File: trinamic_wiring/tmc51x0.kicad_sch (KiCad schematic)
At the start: 0 parts

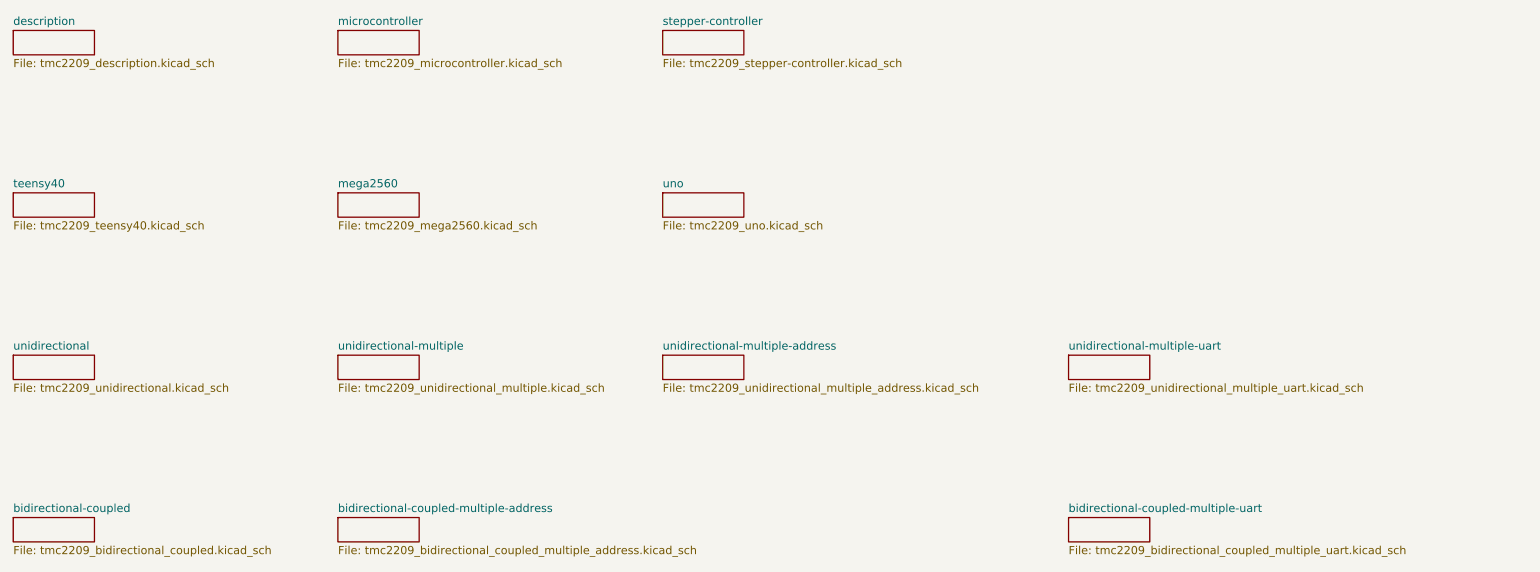
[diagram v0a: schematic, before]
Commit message: Add TMC51X0 files
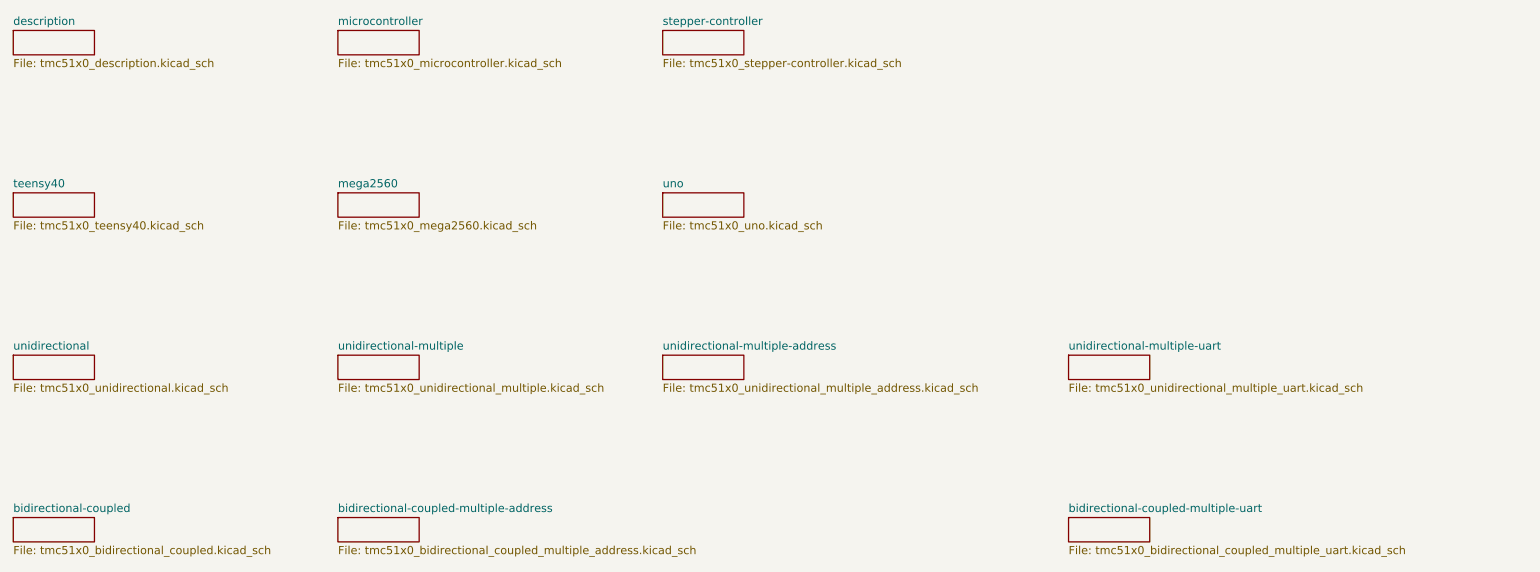
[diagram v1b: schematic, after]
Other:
- sheet bidirectional-coupled: file tmc2209_bidirectional_coupled.kicad_sch -> tmc51x0_bidirectional_coupled.kicad_sch
- sheet bidirectional-coupled-multiple-address: file tmc2209_bidirectional_coupled_multiple_address.kicad_sch -> tmc51x0_bidirectional_coupled_multiple_address.kicad_sch
- sheet bidirectional-coupled-multiple-uart: file tmc2209_bidirectional_coupled_multiple_uart.kicad_sch -> tmc51x0_bidirectional_coupled_multiple_uart.kicad_sch
- sheet description: file tmc2209_description.kicad_sch -> tmc51x0_description.kicad_sch
- sheet mega2560: file tmc2209_mega2560.kicad_sch -> tmc51x0_mega2560.kicad_sch
- sheet microcontroller: file tmc2209_microcontroller.kicad_sch -> tmc51x0_microcontroller.kicad_sch
- sheet stepper-controller: file tmc2209_stepper-controller.kicad_sch -> tmc51x0_stepper-controller.kicad_sch
- sheet teensy40: file tmc2209_teensy40.kicad_sch -> tmc51x0_teensy40.kicad_sch
- sheet unidirectional: file tmc2209_unidirectional.kicad_sch -> tmc51x0_unidirectional.kicad_sch
- sheet unidirectional-multiple: file tmc2209_unidirectional_multiple.kicad_sch -> tmc51x0_unidirectional_multiple.kicad_sch
- sheet unidirectional-multiple-address: file tmc2209_unidirectional_multiple_address.kicad_sch -> tmc51x0_unidirectional_multiple_address.kicad_sch
- sheet unidirectional-multiple-uart: file tmc2209_unidirectional_multiple_uart.kicad_sch -> tmc51x0_unidirectional_multiple_uart.kicad_sch
- sheet uno: file tmc2209_uno.kicad_sch -> tmc51x0_uno.kicad_sch
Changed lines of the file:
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@@
       (effects (font (size 1.27 1.27)) (justify left bottom))
     )
-    (property "Sheetfile" "tmc2209_bidirectional_coupled_multiple_uart.kicad_sch" (at 208.28 133.9346 0)
+    (property "Sheetfile" "tmc51x0_bidirectional_coupled_multiple_uart.kicad_sch" (at 208.28 133.9346 0)
       (effects (font (size 1.27 1.27)) (justify left top))
     )
@@
       (effects (font (size 1.27 1.27)) (justify left bottom))
     )
-    (property "Sheetfile" "tmc2209_unidirectional.kicad_sch" (at 43.18 108.5346 0)
+    (property "Sheetfile" "tmc51x0_unidirectional.kicad_sch" (at 43.18 108.5346 0)
       (effects (font (size 1.27 1.27)) (justify left top))
     )
@@
       (effects (font (size 1.27 1.27)) (justify left bottom))
     )
-    (property "Sheetfile" "tmc2209_stepper-controller.kicad_sch" (at 144.78 57.7346 0)
+    (property "Sheetfile" "tmc51x0_stepper-controller.kicad_sch" (at 144.78 57.7346 0)
       (effects (font (size 1.27 1.27)) (justify left top))
     )
@@
       (effects (font (size 1.27 1.27)) (justify left bottom))
     )
-    (property "Sheetfile" "tmc2209_teensy40.kicad_sch" (at 43.18 83.1346 0)
+    (property "Sheetfile" "tmc51x0_teensy40.kicad_sch" (at 43.18 83.1346 0)
       (effects (font (size 1.27 1.27)) (justify left top))
     )
@@
       (effects (font (size 1.27 1.27)) (justify left bottom))
     )
-    (property "Sheetfile" "tmc2209_unidirectional_multiple.kicad_sch" (at 93.98 108.5346 0)
+    (property "Sheetfile" "tmc51x0_unidirectional_multiple.kicad_sch" (at 93.98 108.5346 0)
       (effects (font (size 1.27 1.27)) (justify left top))
     )
@@
       (effects (font (size 1.27 1.27)) (justify left bottom))
     )
-    (property "Sheetfile" "tmc2209_bidirectional_coupled_multiple_address.kicad_sch" (at 93.98 133.9346 0)
+    (property "Sheetfile" "tmc51x0_bidirectional_coupled_multiple_address.kicad_sch" (at 93.98 133.9346 0)
       (effects (font (size 1.27 1.27)) (justify left top))
     )
@@
       (effects (font (size 1.27 1.27)) (justify left bottom))
     )
-    (property "Sheetfile" "tmc2209_uno.kicad_sch" (at 144.78 83.1346 0)
+    (property "Sheetfile" "tmc51x0_uno.kicad_sch" (at 144.78 83.1346 0)
       (effects (font (size 1.27 1.27)) (justify left top))
     )
@@
       (effects (font (size 1.27 1.27)) (justify left bottom))
     )
-    (property "Sheetfile" "tmc2209_description.kicad_sch" (at 43.18 57.7346 0)
+    (property "Sheetfile" "tmc51x0_description.kicad_sch" (at 43.18 57.7346 0)
       (effects (font (size 1.27 1.27)) (justify left top))
     )
@@
       (effects (font (size 1.27 1.27)) (justify left bottom))
     )
-    (property "Sheetfile" "tmc2209_microcontroller.kicad_sch" (at 93.98 57.7346 0)
+    (property "Sheetfile" "tmc51x0_microcontroller.kicad_sch" (at 93.98 57.7346 0)
       (effects (font (size 1.27 1.27)) (justify left top))
     )
@@
       (effects (font (size 1.27 1.27)) (justify left bottom))
     )
-    (property "Sheetfile" "tmc2209_unidirectional_multiple_address.kicad_sch" (at 144.78 108.5346 0)
+    (property "Sheetfile" "tmc51x0_unidirectional_multiple_address.kicad_sch" (at 144.78 108.5346 0)
       (effects (font (size 1.27 1.27)) (justify left top))
     )
@@
       (effects (font (size 1.27 1.27)) (justify left bottom))
     )
-    (property "Sheetfile" "tmc2209_unidirectional_multiple_uart.kicad_sch" (at 208.28 108.5346 0)
+    (property "Sheetfile" "tmc51x0_unidirectional_multiple_uart.kicad_sch" (at 208.28 108.5346 0)
       (effects (font (size 1.27 1.27)) (justify left top))
     )
@@
       (effects (font (size 1.27 1.27)) (justify left bottom))
     )
-    (property "Sheetfile" "tmc2209_bidirectional_coupled.kicad_sch" (at 43.18 133.9346 0)
+    (property "Sheetfile" "tmc51x0_bidirectional_coupled.kicad_sch" (at 43.18 133.9346 0)
       (effects (font (size 1.27 1.27)) (justify left top))
     )
@@
       (effects (font (size 1.27 1.27)) (justify left bottom))
     )
-    (property "Sheetfile" "tmc2209_mega2560.kicad_sch" (at 93.98 83.1346 0)
+    (property "Sheetfile" "tmc51x0_mega2560.kicad_sch" (at 93.98 83.1346 0)
       (effects (font (size 1.27 1.27)) (justify left top))
     )

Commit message: Remove unused sheets
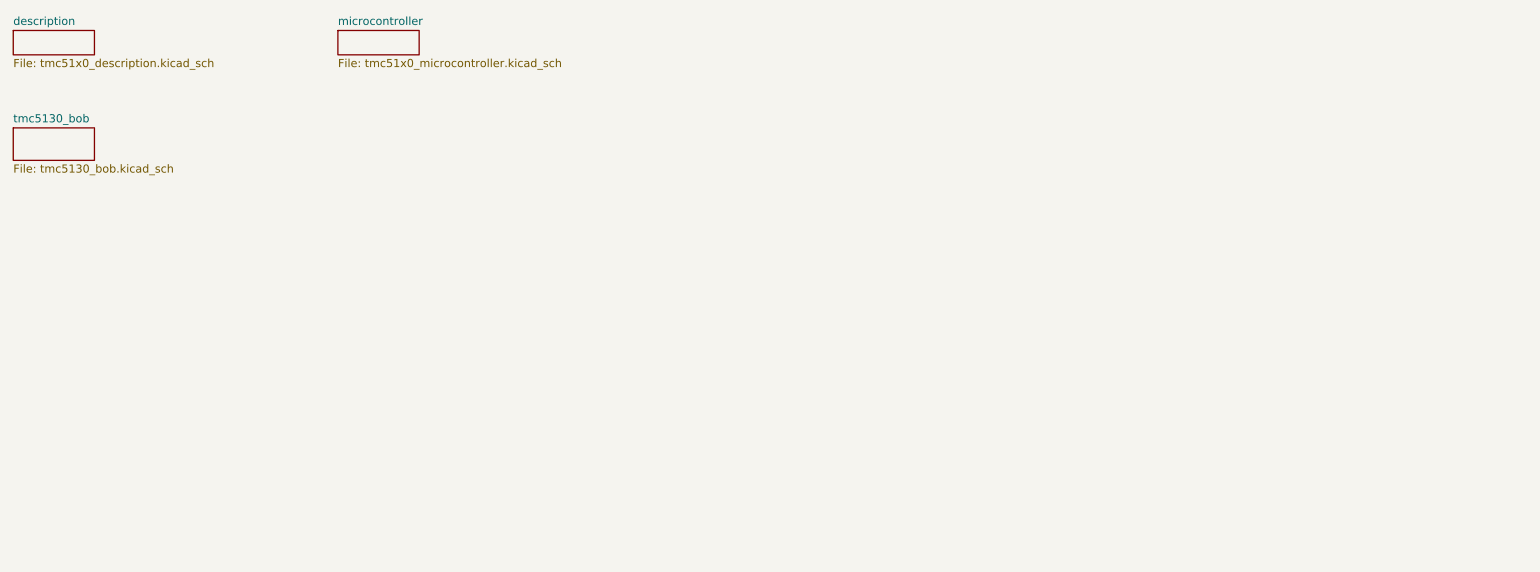
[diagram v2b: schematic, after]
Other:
- removed sheet bidirectional-coupled
- removed sheet bidirectional-coupled-multiple-address
- removed sheet bidirectional-coupled-multiple-uart
- removed sheet mega2560
- removed sheet stepper-controller
- removed sheet teensy40
- removed sheet unidirectional
- removed sheet unidirectional-multiple
- removed sheet unidirectional-multiple-address
- removed sheet unidirectional-multiple-uart
- removed sheet uno
- added sheet tmc5130_bob (tmc5130_bob.kicad_sch)
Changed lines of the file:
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@@
   (title_block
     (title "Trinamic Wiring")
-    (date "2023-08-02")
+    (date "2024-01-31")
     (rev "0.4")
     (company "Janelia Research Campus")
   )
-  (sheet (at 208.28 129.54) (size 12.7 3.81) (fields_autoplaced)
+  (sheet (at 43.18 68.58) (size 12.7 5.08) (fields_autoplaced)
     (stroke (width 0.1524) (type solid))
     (fill (color 0 0 0 0.0000))
-    (property "Sheetname" "bidirectional-coupled-multiple-uart" (at 208.28 128.8284 0)
+    (property "Sheetname" "tmc5130_bob" (at 43.18 67.8684 0)
       (effects (font (size 1.27 1.27)) (justify left bottom))
     )
-    (property "Sheetfile" "tmc51x0_bidirectional_coupled_multiple_uart.kicad_sch" (at 208.28 133.9346 0)
+    (property "Sheetfile" "tmc5130_bob.kicad_sch" (at 43.18 74.2446 0)
       (effects (font (size 1.27 1.27)) (justify left top))
     )
     (instances
       (project "trinamic_wiring"
-        (path "/e4144788-6304-493f-818e-5d881d3b7418/c8eda2b5-ab13-4033-82d9-875c9fcaf884" (page "12"))
-        (path "/e4144788-6304-493f-818e-5d881d3b7418/a161638e-a96f-4455-865a-1d7502675f43" (page "21"))
-      )
-    )
-  )
-  (sheet (at 43.18 104.14) (size 12.7 3.81) (fields_autoplaced)
-    (stroke (width 0.1524) (type solid))
-    (fill (color 0 0 0 0.0000))
-    (property "Sheetname" "unidirectional" (at 43.18 103.4284 0)
-      (effects (font (size 1.27 1.27)) (justify left bottom))
-    )
-    (property "Sheetfile" "tmc51x0_unidirectional.kicad_sch" (at 43.18 108.5346 0)
-      (effects (font (size 1.27 1.27)) (justify left top))
-    )
-    (instances
-      (project "trinamic_wiring"
-        (path "/e4144788-6304-493f-818e-5d881d3b7418/c8eda2b5-ab13-4033-82d9-875c9fcaf884" (page "6"))
-        (path "/e4144788-6304-493f-818e-5d881d3b7418/a161638e-a96f-4455-865a-1d7502675f43" (page "18"))
-      )
-    )
-  )
-  (sheet (at 144.78 53.34) (size 12.7 3.81) (fields_autoplaced)
-    (stroke (width 0.1524) (type solid))
-    (fill (color 0 0 0 0.0000))
-    (property "Sheetname" "stepper-controller" (at 144.78 52.6284 0)
-      (effects (font (size 1.27 1.27)) (justify left bottom))
-    )
-    (property "Sheetfile" "tmc51x0_stepper-controller.kicad_sch" (at 144.78 57.7346 0)
-      (effects (font (size 1.27 1.27)) (justify left top))
-    )
-    (instances
-      (project "trinamic_wiring"
-        (path "/e4144788-6304-493f-818e-5d881d3b7418/c8eda2b5-ab13-4033-82d9-875c9fcaf884" (page "15"))
-        (path "/e4144788-6304-493f-818e-5d881d3b7418/a161638e-a96f-4455-865a-1d7502675f43" (page "28"))
-      )
-    )
-  )
-  (sheet (at 43.18 78.74) (size 12.7 3.81) (fields_autoplaced)
-    (stroke (width 0.1524) (type solid))
-    (fill (color 0 0 0 0.0000))
-    (property "Sheetname" "teensy40" (at 43.18 78.0284 0)
-      (effects (font (size 1.27 1.27)) (justify left bottom))
-    )
-    (property "Sheetfile" "tmc51x0_teensy40.kicad_sch" (at 43.18 83.1346 0)
-      (effects (font (size 1.27 1.27)) (justify left top))
-    )
-    (instances
-      (project "trinamic_wiring"
-        (path "/e4144788-6304-493f-818e-5d881d3b7418/c8eda2b5-ab13-4033-82d9-875c9fcaf884" (page "3"))
-        (path "/e4144788-6304-493f-818e-5d881d3b7418/a161638e-a96f-4455-865a-1d7502675f43" (page "27"))
-      )
-    )
-  )
-  (sheet (at 93.98 104.14) (size 12.7 3.81) (fields_autoplaced)
-    (stroke (width 0.1524) (type solid))
-    (fill (color 0 0 0 0.0000))
-    (property "Sheetname" "unidirectional-multiple" (at 93.98 103.4284 0)
-      (effects (font (size 1.27 1.27)) (justify left bottom))
-    )
-    (property "Sheetfile" "tmc51x0_unidirectional_multiple.kicad_sch" (at 93.98 108.5346 0)
-      (effects (font (size 1.27 1.27)) (justify left top))
-    )
-    (instances
-      (project "trinamic_wiring"
-        (path "/e4144788-6304-493f-818e-5d881d3b7418/c8eda2b5-ab13-4033-82d9-875c9fcaf884" (page "8"))
-        (path "/e4144788-6304-493f-818e-5d881d3b7418/a161638e-a96f-4455-865a-1d7502675f43" (page "22"))
-      )
-    )
-  )
-  (sheet (at 93.98 129.54) (size 12.7 3.81) (fields_autoplaced)
-    (stroke (width 0.1524) (type solid))
-    (fill (color 0 0 0 0.0000))
-    (property "Sheetname" "bidirectional-coupled-multiple-address" (at 93.98 128.8284 0)
-      (effects (font (size 1.27 1.27)) (justify left bottom))
-    )
-    (property "Sheetfile" "tmc51x0_bidirectional_coupled_multiple_address.kicad_sch" (at 93.98 133.9346 0)
-      (effects (font (size 1.27 1.27)) (justify left top))
-    )
-    (instances
-      (project "trinamic_wiring"
-        (path "/e4144788-6304-493f-818e-5d881d3b7418/c8eda2b5-ab13-4033-82d9-875c9fcaf884" (page "5"))
-        (path "/e4144788-6304-493f-818e-5d881d3b7418/a161638e-a96f-4455-865a-1d7502675f43" (page "20"))
-      )
-    )
-  )
-  (sheet (at 144.78 78.74) (size 12.7 3.81) (fields_autoplaced)
-    (stroke (width 0.1524) (type solid))
-    (fill (color 0 0 0 0.0000))
-    (property "Sheetname" "uno" (at 144.78 78.0284 0)
-      (effects (font (size 1.27 1.27)) (justify left bottom))
-    )
-    (property "Sheetfile" "tmc51x0_uno.kicad_sch" (at 144.78 83.1346 0)
-      (effects (font (size 1.27 1.27)) (justify left top))
-    )
-    (instances
-      (project "trinamic_wiring"
-        (path "/e4144788-6304-493f-818e-5d881d3b7418/c8eda2b5-ab13-4033-82d9-875c9fcaf884" (page "10"))
-        (path "/e4144788-6304-493f-818e-5d881d3b7418/a161638e-a96f-4455-865a-1d7502675f43" (page "24"))
+        (path "/e4144788-6304-493f-818e-5d881d3b7418/a161638e-a96f-4455-865a-1d7502675f43" (page "30"))
       )
     )
@@
       )
     )
-  )
-  (sheet (at 144.78 104.14) (size 12.7 3.81) (fields_autoplaced)
-    (stroke (width 0.1524) (type solid))
-    (fill (color 0 0 0 0.0000))
-    (property "Sheetname" "unidirectional-multiple-address" (at 144.78 103.4284 0)
-      (effects (font (size 1.27 1.27)) (justify left bottom))
-    )
-    (property "Sheetfile" "tmc51x0_unidirectional_multiple_address.kicad_sch" (at 144.78 108.5346 0)
-      (effects (font (size 1.27 1.27)) (justify left top))
-    )
-    (instances
-      (project "trinamic_wiring"
-        (path "/e4144788-6304-493f-818e-5d881d3b7418/c8eda2b5-ab13-4033-82d9-875c9fcaf884" (page "9"))
-        (path "/e4144788-6304-493f-818e-5d881d3b7418/a161638e-a96f-4455-865a-1d7502675f43" (page "25"))
-      )
-    )
-  )
-  (sheet (at 208.28 104.14) (size 12.7 3.81) (fields_autoplaced)
-    (stroke (width 0.1524) (type solid))
-    (fill (color 0 0 0 0.0000))
-    (property "Sheetname" "unidirectional-multiple-uart" (at 208.28 103.4284 0)
-      (effects (font (size 1.27 1.27)) (justify left bottom))
-    )
-    (property "Sheetfile" "tmc51x0_unidirectional_multiple_uart.kicad_sch" (at 208.28 108.5346 0)
-      (effects (font (size 1.27 1.27)) (justify left top))
-    )
-    (instances
-      (project "trinamic_wiring"
-        (path "/e4144788-6304-493f-818e-5d881d3b7418/c8eda2b5-ab13-4033-82d9-875c9fcaf884" (page "11"))
-        (path "/e4144788-6304-493f-818e-5d881d3b7418/a161638e-a96f-4455-865a-1d7502675f43" (page "26"))
-      )
-    )
-  )
-  (sheet (at 43.18 129.54) (size 12.7 3.81) (fields_autoplaced)
-    (stroke (width 0.1524) (type solid))
-    (fill (color 0 0 0 0.0000))
-    (property "Sheetname" "bidirectional-coupled" (at 43.18 128.8284 0)
-      (effects (font (size 1.27 1.27)) (justify left bottom))
-    )
-    (property "Sheetfile" "tmc51x0_bidirectional_coupled.kicad_sch" (at 43.18 133.9346 0)
-      (effects (font (size 1.27 1.27)) (justify left top))
-    )
-    (instances
-      (project "trinamic_wiring"
-        (path "/e4144788-6304-493f-818e-5d881d3b7418/c8eda2b5-ab13-4033-82d9-875c9fcaf884" (page "7"))
-        (path "/e4144788-6304-493f-818e-5d881d3b7418/a161638e-a96f-4455-865a-1d7502675f43" (page "23"))
-      )
-    )
-  )
-  (sheet (at 93.98 78.74) (size 12.7 3.81) (fields_autoplaced)
-    (stroke (width 0.1524) (type solid))
-    (fill (color 0 0 0 0.0000))
-    (property "Sheetname" "mega2560" (at 93.98 78.0284 0)
-      (effects (font (size 1.27 1.27)) (justify left bottom))
-    )
-    (property "Sheetfile" "tmc51x0_mega2560.kicad_sch" (at 93.98 83.1346 0)
-      (effects (font (size 1.27 1.27)) (justify left top))
-    )
-    (instances
-      (project "trinamic_wiring"
-        (path "/e4144788-6304-493f-818e-5d881d3b7418/c8eda2b5-ab13-4033-82d9-875c9fcaf884" (page "4"))
-        (path "/e4144788-6304-493f-818e-5d881d3b7418/a161638e-a96f-4455-865a-1d7502675f43" (page "17"))
-      )
-    )

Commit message: Rename bob
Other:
- sheet tmc5130_bob renamed tmc51x0_bob
- sheet tmc51x0_bob: file tmc5130_bob.kicad_sch -> tmc51x0_bob.kicad_sch
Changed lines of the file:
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@@
     (stroke (width 0.1524) (type solid))
     (fill (color 0 0 0 0.0000))
-    (property "Sheetname" "tmc5130_bob" (at 43.18 67.8684 0)
+    (property "Sheetname" "tmc51x0_bob" (at 43.18 67.8684 0)
       (effects (font (size 1.27 1.27)) (justify left bottom))
     )
-    (property "Sheetfile" "tmc5130_bob.kicad_sch" (at 43.18 74.2446 0)
+    (property "Sheetfile" "tmc51x0_bob.kicad_sch" (at 43.18 74.2446 0)
       (effects (font (size 1.27 1.27)) (justify left top))
     )
